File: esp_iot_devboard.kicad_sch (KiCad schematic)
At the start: 0 parts

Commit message: Add USB-C power and local library setup
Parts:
- added J?: B2B-PH-SM4-TB, B2B-PH-SM4-TB:JST_B2B-PH-SM4-TB, symbol B2B-PH-SM4-TB:B2B-PH-SM4-TB
- added J?: SS-52400-002, SS-52400-002:BELFUSE_SS-52400-002, symbol SS-52400-002:SS-52400-002
- added R? (x2): 5k1, symbol Device:R
- added U?: MCP73871-2CAI_ML, MCP73871-2CAI_ML:QFN50P400X400X100-21N, symbol MCP73871-2CAI_ML:MCP73871-2CAI_ML
- added VR?: LM1117MPX-3.3_NOPB, LM1117MPX-3.3_NOPB:VREG_LM1117MPX-3.3_NOPB, symbol LM1117MPX-3.3_NOPB:LM1117MPX-3.3_NOPB
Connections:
- new net: J?.A5 (CC1), R?.1
- new net: U?.1 (OUT), U?.20 (OUT)
- new net: U?.10 (VSS), U?.11 (VSS), U?.21 (VSS)
- new net: U?.14 (VBAT), U?.15 (VBAT)
- new net: U?.18 (IN), U?.19 (IN)
- new net: J?.B5 (CC2), R?.1
- new net: J?.G1 (GND/SHIELD), J?.G2 (GND/SHIELD), J?.G3 (GND/SHIELD), J?.G4 (GND/SHIELD), J?.S1 (GND/SHIELD), J?.S2 (GND/SHIELD), J?.S3 (GND/SHIELD), J?.S4 (GND/SHIELD)
- new net GND: R?.2, R?.2
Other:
- title: (none) -> ESP32 sensor board - Root

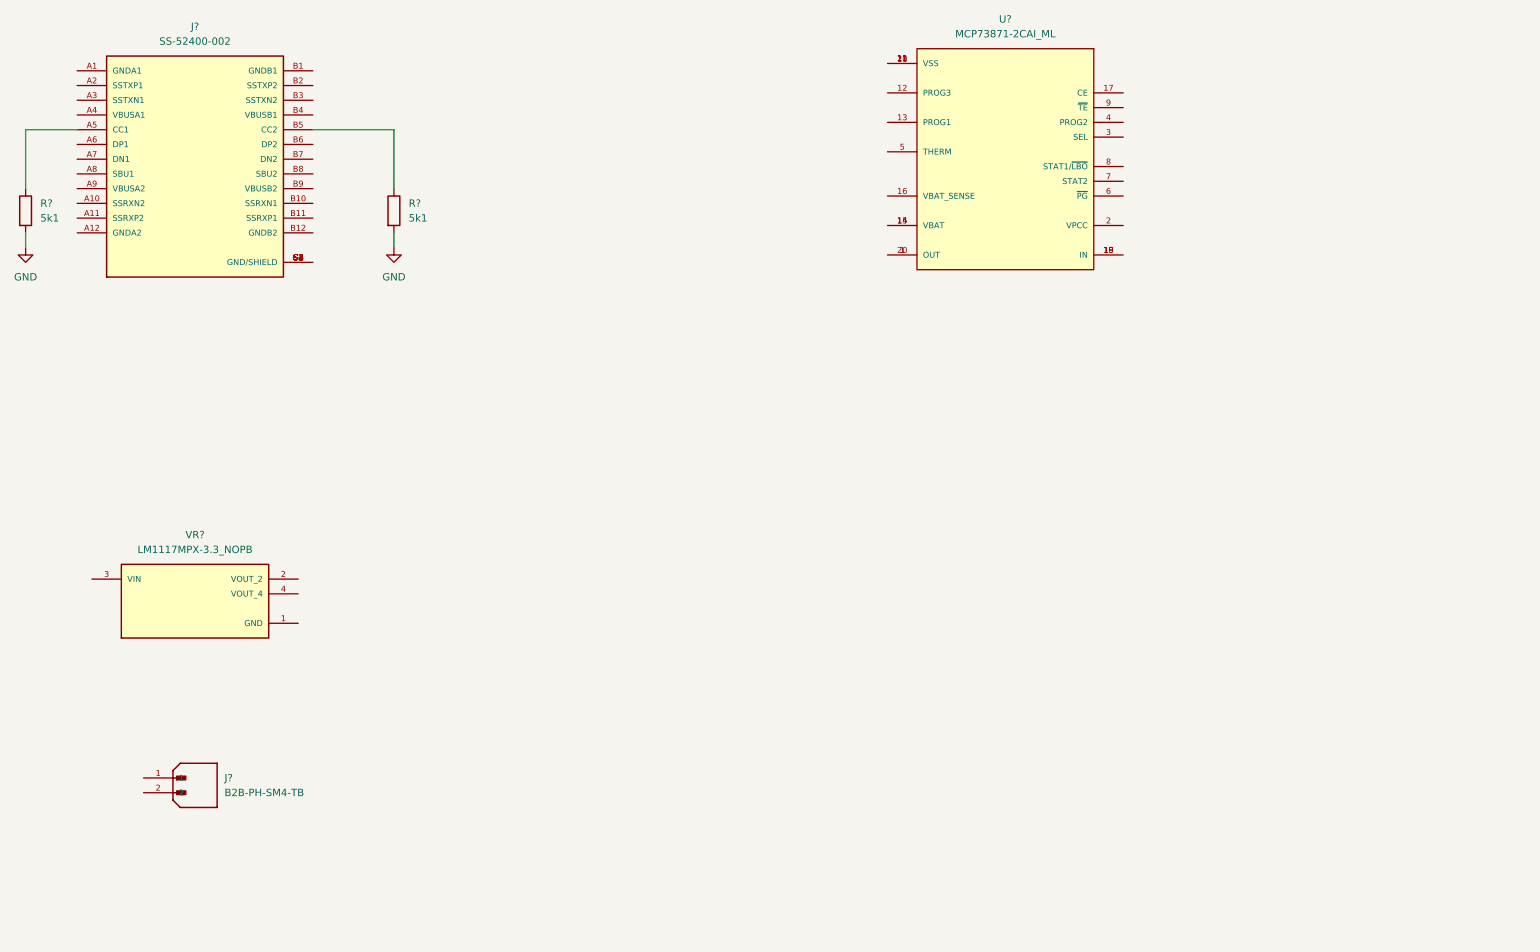
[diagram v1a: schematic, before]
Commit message: Connect USB receptacle and LiPo battery charger
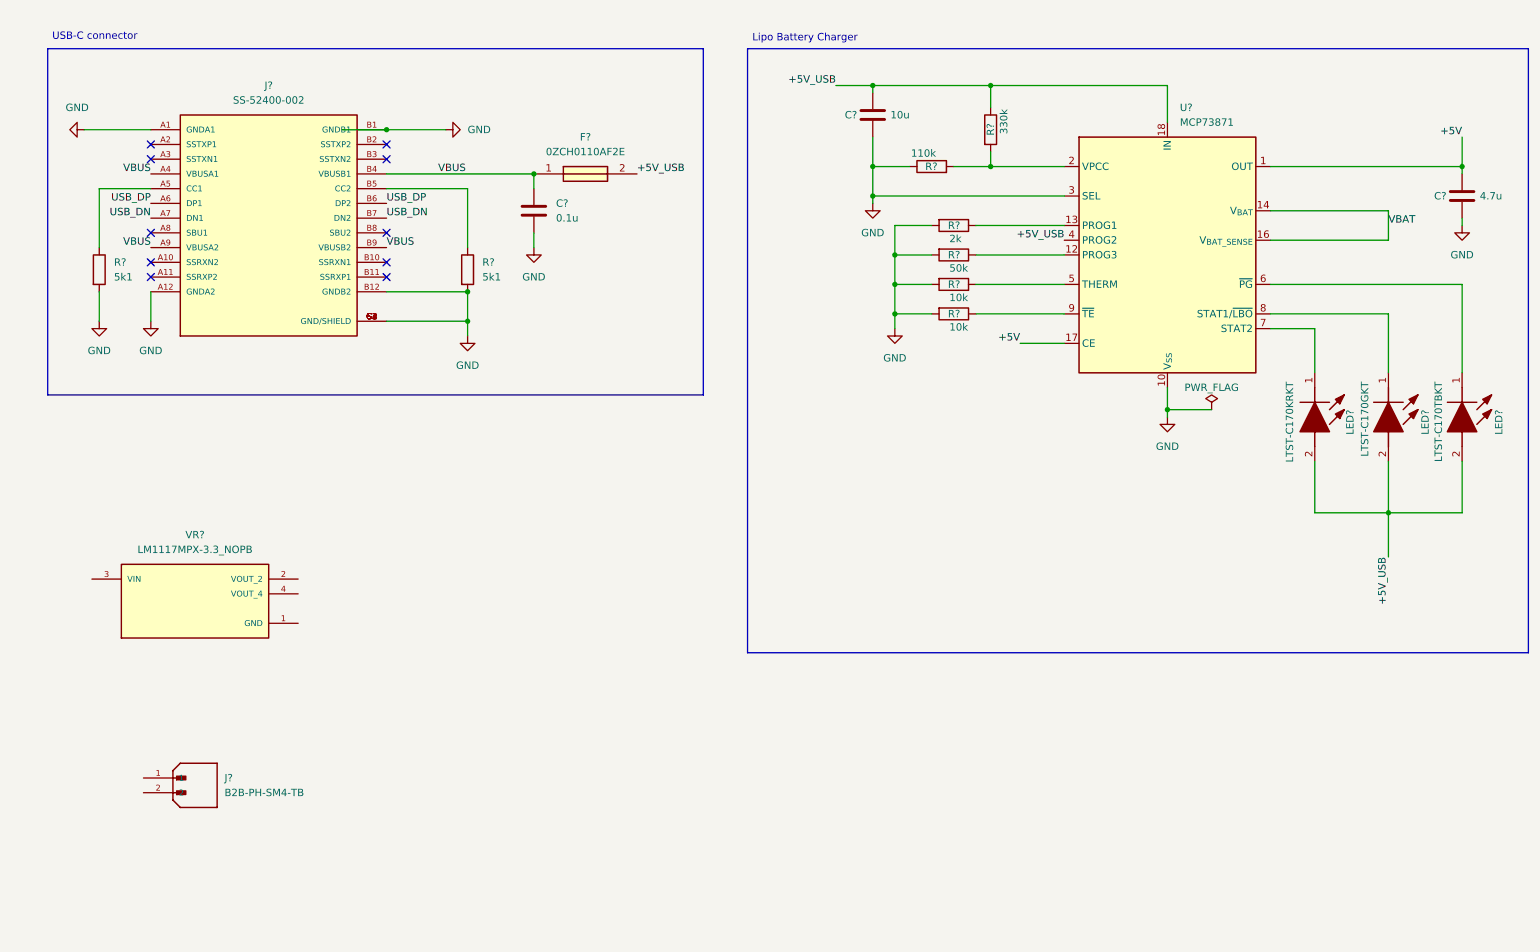
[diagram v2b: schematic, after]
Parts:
- removed U?: MCP73871-2CAI_ML, MCP73871-2CAI_ML:QFN50P400X400X100-21N, symbol MCP73871-2CAI_ML:MCP73871-2CAI_ML
- added C?: 10u, symbol Device:C
- added C?: 0.1u, symbol Device:C
- added C?: 4.7u, symbol Device:C
- added F?: 0ZCH0110AF2E, FUSC3226X100N, symbol 0ZCH0110AF2E:0ZCH0110AF2E
- added LED?: LTST-C170KRKT, LEDC2012X120N, symbol LTST-C170KRKT:LTST-C170KRKT
- added LED?: LTST-C170GKT, LEDC2012X120N, symbol LTST-C170GKT:LTST-C170GKT
- added LED?: LTST-C170TBKT, LEDC2012X120N, symbol LTST-C170TBKT:LTST-C170TBKT
- added R? (x2): 10k, symbol Device:R
- added R?: 110k, symbol Device:R
- added R?: 50k, symbol Device:R
- added R?: 2k, symbol Device:R
- added R?: 330k, symbol Device:R
- added U?: MCP73871, Package_DFN_QFN:QFN-20-1EP_4x4mm_P0.5mm_EP2.5x2.5mm, symbol Battery_Management:MCP73871
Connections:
- net GND: now also J?.A1 (GNDA1), J?.A12 (GNDA2), J?.B1 (GNDB1), J?.B12 (GNDB2), J?.G1 (GND/SHIELD), J?.G2 (GND/SHIELD), J?.G3 (GND/SHIELD), J?.G4 (GND/SHIELD), J?.S1 (GND/SHIELD), J?.S2 (GND/SHIELD), J?.S3 (GND/SHIELD), J?.S4 (GND/SHIELD), C?.2, C?.2, C?.2, R?.1, R?.2, R?.2, R?.2, R?.2, U?.10 (V_{SS}), U?.11 (V_{SS}), U?.21 (V_{SS}), U?.3 (SEL)
- net VBUS: now reaches J?.A4 (VBUSA1)
- net VBUS: now also J?.A9 (VBUSA2), J?.B4 (VBUSB1), J?.B9 (VBUSB2), C?.1, F?.1
- net USB_DP: now reaches J?.A6 (DP1)
- net USB_DP: now also J?.B6 (DP2)
- net USB_DN: now reaches J?.A7 (DN1)
- net USB_DN: now also J?.B7 (DN2)
- new net: LED?.1 (K), U?.7 (STAT2)
- new net: LED?.1 (K), U?.8 (STAT1/~{LBO})
- new net: R?.1, U?.5 (THERM)
- new net: LED?.1 (K), U?.6 (~{PG})
- new net: R?.1, U?.9 (~{TE})
- new net: R?.2, R?.2, U?.2 (VPCC)
- new net: R?.1, U?.12 (PROG3)
- new net: R?.1, U?.13 (PROG1)
- new net +5V: C?.1, U?.1 (OUT), U?.17 (CE), U?.20 (OUT)
- new net +5V_USB: C?.1, F?.2, LED?.2 (A), LED?.2 (A), LED?.2 (A), R?.1, U?.18 (IN), U?.19 (IN), U?.4 (PROG2)
- new net VBAT: U?.14 (V_{BAT}), U?.15 (V_{BAT}), U?.16 (V_{BAT_SENSE})
- no-connect marks 0 -> 10
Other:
- note added: "Lipo Battery Charger"
- note added: "USB-C connector"
- moved on the sheet: J?, R?

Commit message: Complete first schematic page
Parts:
- added C? (x2): 10u, symbol Device:C_Polarized
- added C? (x2): 0.1u, symbol Device:C
- added LED?: LTST-C170KRKT, LEDC2012X120N, symbol LTST-C170KRKT:LTST-C170KRKT
- added R? (x4): 470k, symbol Device:R
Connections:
- net +5V: now also VR?.3 (VIN), C?.1, C?.1; no longer U?.17 (CE)
- net +5V_USB: now also U?.17 (CE)
- net GND: now also J?.1, VR?.1 (GND), C?.2, C?.2, C?.2, C?.2, R?.1
- net VBAT: now also J?.2
- net at LED?.1 (K): now also R?.2; no longer U?.7 (STAT2)
- net at LED?.1 (K): now also R?.2; no longer U?.8 (STAT1/~{LBO})
- net +3.3V: now reaches VR?.2 (VOUT_2)
- net +3.3V: now also VR?.4 (VOUT_4), C?.1, C?.1, LED?.2 (A)
- net at U?.6 (~{PG}): now also R?.1; no longer LED?.1 (K)
- new net: LED?.1 (K), R?.2
- new net: R?.1, U?.7 (STAT2)
- new net: R?.1, U?.8 (STAT1/~{LBO})
- new net PWD_LED: LED?.1 (K), R?.2
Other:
- note added: "Battery JST Connector"
- note added: "Low Dropout Voltage Regulator"
- note added: "Power LED"
- moved on the sheet: J?, LED?, VR?

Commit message: Add ESP32-C3 schematic sheet and USB interface references
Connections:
- net at LED?.1 (K): now also R?.2; no longer R?.2 (x2)
- net CHARGING_POWER_GOOD: now reaches R?.1, U?.6 (~{PG})
- net CHARGING: now reaches R?.1, U?.7 (STAT2)
- net CHARGED: now reaches R?.1, U?.8 (STAT1/~{LBO})
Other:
- added sheet ESP32-C3-02 (esp32-c3-02.kicad_sch)
- moved on the sheet: LED?
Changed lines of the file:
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@@
 	(wire
 		(pts
-			(xy 238.76 100.33) (xy 238.76 109.22)
-		)
-		(stroke
-			(width 0)
-			(type default)
-		)
-	)
-	(wire
-		(pts
-			(xy 238.76 78.74) (xy 238.76 85.09)
+			(xy 234.95 135.89) (xy 227.33 135.89)
 		)
 		(stroke
@@
 	(wire
 		(pts
-			(xy 251.46 78.74) (xy 251.46 85.09)
-		)
-		(stroke
-			(width 0)
-			(type default)
-		)
-	)
-	(wire
-		(pts
 			(xy 116.84 114.3) (xy 109.22 114.3)
 		)
@@
 	(wire
 		(pts
+			(xy 264.16 100.33) (xy 264.16 109.22)
+		)
+		(stroke
+			(width 0)
+			(type default)
+		)
+	)
+	(wire
+		(pts
+			(xy 238.76 78.74) (xy 238.76 85.09)
+		)
+		(stroke
+			(width 0)
+			(type default)
+		)
+	)
+	(wire
+		(pts
 			(xy 182.88 40.64) (xy 195.58 40.64)
 		)
@@
 	(wire
 		(pts
-			(xy 251.46 100.33) (xy 251.46 109.22)
+			(xy 251.46 78.74) (xy 251.46 85.09)
 		)
 		(stroke
@@
 	(wire
 		(pts
-			(xy 264.16 100.33) (xy 264.16 109.22)
+			(xy 264.16 78.74) (xy 264.16 85.09)
 		)
 		(stroke
@@
 	(wire
 		(pts
-			(xy 55.88 111.76) (xy 55.88 114.3)
+			(xy 227.33 133.35) (xy 234.95 133.35)
 		)
 		(stroke
@@
 	(wire
 		(pts
-			(xy 104.14 52.07) (xy 104.14 54.61)
+			(xy 55.88 111.76) (xy 55.88 114.3)
 		)
 		(stroke
@@
 	(wire
 		(pts
-			(xy 78.74 34.29) (xy 88.9 34.29)
+			(xy 104.14 52.07) (xy 104.14 54.61)
 		)
 		(stroke
@@
 	(wire
 		(pts
-			(xy 231.14 60.96) (xy 264.16 60.96)
+			(xy 78.74 34.29) (xy 88.9 34.29)
 		)
 		(stroke
@@
 	(wire
 		(pts
-			(xy 116.84 101.6) (xy 116.84 104.14)
+			(xy 231.14 60.96) (xy 264.16 60.96)
 		)
 		(stroke
@@
 	(wire
 		(pts
-			(xy 149.86 137.16) (xy 149.86 140.97)
+			(xy 116.84 101.6) (xy 116.84 104.14)
 		)
 		(stroke
@@
 	(wire
 		(pts
-			(xy 77.47 151.13) (xy 81.28 151.13)
+			(xy 149.86 137.16) (xy 149.86 140.97)
 		)
 		(stroke
@@
 	(wire
 		(pts
-			(xy 102.87 101.6) (xy 102.87 104.14)
+			(xy 77.47 151.13) (xy 81.28 151.13)
 		)
 		(stroke
@@
 	(wire
 		(pts
-			(xy 264.16 78.74) (xy 264.16 85.09)
+			(xy 102.87 101.6) (xy 102.87 104.14)
 		)
 		(stroke
@@
 	(wire
 		(pts
+			(xy 251.46 100.33) (xy 251.46 109.22)
+		)
+		(stroke
+			(width 0)
+			(type default)
+		)
+	)
+	(wire
+		(pts
 			(xy 172.72 50.8) (xy 166.37 50.8)
 		)
@@
 	(wire
 		(pts
+			(xy 238.76 100.33) (xy 238.76 109.22)
+		)
+		(stroke
+			(width 0)
+			(type default)
+		)
+	)
+	(wire
+		(pts
 			(xy 109.22 118.11) (xy 109.22 114.3)
 		)
@@
 	)
 	(label "USB_DN"
+		(at 234.95 133.35 0)
+		(effects
+			(font
+				(size 1.27 1.27)
+			)
+			(justify left bottom)
+		)
+	)
+	(label "USB_DN"
 		(at 78.74 49.53 0)
 		(effects
@@
 		)
 	)
+	(label "USB_DP"
+		(at 234.95 135.89 0)
+		(effects
+			(font
+				(size 1.27 1.27)
+			)
+			(justify left bottom)
+		)
+	)
+	(label "CHARGED"
+		(at 251.46 66.04 180)
+		(effects
+			(font
+				(size 1.27 1.27)
+			)
+			(justify right bottom)
+		)
+	)
 	(label "+5V_USB"
 		(at 251.46 114.3 270)
@@
 		)
 	)
+	(label "CHARGING_POWER_GOOD"
+		(at 264.16 60.96 180)
+		(effects
+			(font
+				(size 1.27 1.27)
+			)
+			(justify right bottom)
+		)
+	)
 	(label "USB_DP"
 		(at 78.74 46.99 0)
@@
 		)
 	)
+	(label "CHARGING"
+		(at 238.76 68.58 0)
+		(effects
+			(font
+				(size 1.27 1.27)
+			)
+			(justify left bottom)
+		)
+	)
 	(symbol
 		(lib_id "power:GND")
@@
 	(symbol
 		(lib_id "LTST-C170KRKT:LTST-C170KRKT")
-		(at 238.76 85.09 270)
+		(at 264.16 85.09 270)
 		(unit 1)
 		(exclude_from_sim no)
@@
 		(dnp no)
 		(property "Reference" "LED?"
-			(at 244.856 91.44 0)
+			(at 270.256 91.44 0)
 			(effects
 				(font
@@
 		)
 		(property "Value" "LTST-C170KRKT"
-			(at 234.442 86.614 0)
+			(at 259.842 86.614 0)
 			(effects
 				(font
@@
 		)
 		(property "Footprint" "LEDC2012X120N"
-			(at 145.11 97.79 0)
+			(at 170.51 97.79 0)
 			(effects
 				(font
@@
 		)
 		(property "Datasheet" "https://componentsearchengine.com/Datasheets/1/LTST-C170KRKT.pdf"
-			(at 45.11 97.79 0)
+			(at 70.51 97.79 0)
 			(effects
 				(font
@@
 		)
 		(property "Description" "Standard LEDs - SMD Red Clear 631nm"
-			(at 238.76 85.09 0)
+			(at 264.16 85.09 0)
 			(effects
 				(font
@@
 		)
 		(property "Height" "1.2"
-			(at -154.89 97.79 0)
+			(at -129.49 97.79 0)
 			(effects
 				(font
@@
 		)
 		(property "Manufacturer_Name" "Lite-On"
-			(at -254.89 97.79 0)
+			(at -229.49 97.79 0)
 			(effects
 				(font
@@
 		)
 		(property "Manufacturer_Part_Number" "LTST-C170KRKT"
-			(at -354.89 97.79 0)
+			(at -329.49 97.79 0)
 			(effects
 				(font
@@
 		)
 		(property "Mouser Part Number" "859-LTST-C170KRKT"
-			(at -454.89 97.79 0)
+			(at -429.49 97.79 0)
 			(effects
 				(font
@@
 		)
 		(property "Mouser Price/Stock" "https://www.mouser.co.uk/ProductDetail/Lite-On/LTST-C170KRKT?qs=NUb82WqeCyrVOID%2Fxt4rgA%3D%3D"
-			(at -554.89 97.79 0)
+			(at -529.49 97.79 0)
 			(effects
 				(font
@@
 		)
 		(property "Arrow Part Number" "LTST-C170KRKT"
-			(at -654.89 97.79 0)
+			(at -629.49 97.79 0)
 			(effects
 				(font
@@
 		)
 		(property "Arrow Price/Stock" "https://www.arrow.com/en/products/ltst-c170krkt/lite-on-technology?utm_currency=USD&region=nac"
-			(at -754.89 97.79 0)
+			(at -729.49 97.79 0)
 			(effects
 				(font
@@
 	(symbol
 		(lib_id "LTST-C170TBKT:LTST-C170TBKT")
-		(at 264.16 85.09 270)
+		(at 238.76 85.09 270)
 		(unit 1)
 		(exclude_from_sim no)
@@
 		(dnp no)
 		(property "Reference" "LED?"
-			(at 270.51 91.4399 0)
+			(at 245.11 91.4399 0)
 			(effects
 				(font
@@
 		)
 		(property "Value" "LTST-C170TBKT"
-			(at 260.096 86.614 0)
+			(at 234.696 86.614 0)
 			(effects
 				(font
@@
 		)
 		(property "Footprint" "LEDC2012X120N"
-			(at 170.51 97.79 0)
+			(at 145.11 97.79 0)
 			(effects
 				(font
@@
 		)
 		(property "Datasheet" "https://componentsearchengine.com/Datasheets/1/LTST-C170TBKT.pdf"
-			(at 70.51 97.79 0)
+			(at 45.11 97.79 0)
 			(effects
 				(font
@@
 		)
 		(property "Description" "LED,SMD,0805,Blue,28mcd,130deg"
-			(at 264.16 85.09 0)
+			(at 238.76 85.09 0)
 			(effects
 				(font
@@
 		)
 		(property "Height" "1.2"
-			(at -129.49 97.79 0)
+			(at -154.89 97.79 0)
 			(effects
 				(font
@@
 		)
 		(property "Manufacturer_Name" "Lite-On"
-			(at -229.49 97.79 0)
+			(at -254.89 97.79 0)
 			(effects
 				(font
@@
 		)
 		(property "Manufacturer_Part_Number" "LTST-C170TBKT"
-			(at -329.49 97.79 0)
+			(at -354.89 97.79 0)
 			(effects
 				(font
@@
 		)
 		(property "Mouser Part Number" "859-LTST-C170TBKT"
-			(at -429.49 97.79 0)
+			(at -454.89 97.79 0)
 			(effects
 				(font
@@
 		)
 		(property "Mouser Price/Stock" "https://www.mouser.co.uk/ProductDetail/Lite-On/LTST-C170TBKT?qs=0uL0gcxEMop2ooGmIUzw3A%3D%3D"
-			(at -529.49 97.79 0)
+			(at -554.89 97.79 0)
 			(effects
 				(font
@@
 		)
 		(property "Arrow Part Number" "LTST-C170TBKT"
-			(at -629.49 97.79 0)
+			(at -654.89 97.79 0)
 			(effects
 				(font
@@
 		)
 		(property "Arrow Price/Stock" "https://www.arrow.com/en/products/ltst-c170tbkt/lite-on-technology?utm_currency=USD&region=nac"
-			(at -729.49 97.79 0)
+			(at -754.89 97.79 0)
 			(effects
 				(font
@@
 				)
 			)
+		)
+	)
+	(sheet
+		(at 201.93 129.54)
+		(size 25.4 22.86)
+		(exclude_from_sim no)
+		(in_bom yes)
+		(on_board yes)
+		(dnp no)
+		(fields_autoplaced yes)
+		(stroke
+			(width 0.1524)
+			(type solid)
+		)
+		(fill
+			(color 255 91 92 1.0000)
+		)
+		(property "Sheetname" "ESP32-C3-02"
+			(at 201.93 128.8284 0)
+			(effects
+				(font
+					(size 1.27 1.27)
+				)
+				(justify left bottom)
+			)
+		)
+		(property "Sheetfile" "esp32-c3-02.kicad_sch"
+			(at 201.93 152.9846 0)
+			(effects
+				(font
+					(size 1.27 1.27)
+				)
+				(justify left top)
+			)
+		)
+		(pin "USB_DN" input
+			(at 227.33 133.35 0)
+			(effects
+				(font
+					(size 1.27 1.27)
+				)
+				(justify right)
+			)
+		)
+		(pin "USB_DP" input
+			(at 227.33 135.89 0)
+			(effects
+				(font
+					(size 1.27 1.27)
+				)
+				(justify right)
+			)
+		)
+		(instances
+			(project "esp_iot_devboard"
+				(path "/d22eb29f-b1fe-4eb9-837e-233adf238f06"
+					(page "2")
+				)
+			)

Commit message: Wire USB-to-UART module
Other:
- sheet ESP32-C3-02 ports: added VBUS; removed none
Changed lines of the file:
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@@
 	(wire
 		(pts
+			(xy 227.33 138.43) (xy 234.95 138.43)
+		)
+		(stroke
+			(width 0)
+			(type default)
+		)
+	)
+	(wire
+		(pts
 			(xy 231.14 66.04) (xy 251.46 66.04)
 		)
@@
 		)
 	)
+	(label "VBUS"
+		(at 234.95 138.43 0)
+		(effects
+			(font
+				(size 1.27 1.27)
+			)
+			(justify left bottom)
+		)
+	)
 	(label "USB_DN"
 		(at 78.74 49.53 0)
@@
 			(effects
 				(font
+					(size 1.27 1.27)
+				)
+				(justify right)
+			)
+		)
+		(pin "VBUS" input
+			(at 227.33 138.43 0)
+			(effects
+				(font
